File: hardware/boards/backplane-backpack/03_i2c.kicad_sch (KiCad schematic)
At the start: 13 parts, among them J11 backplane_mate, U2 TCA9548APWR

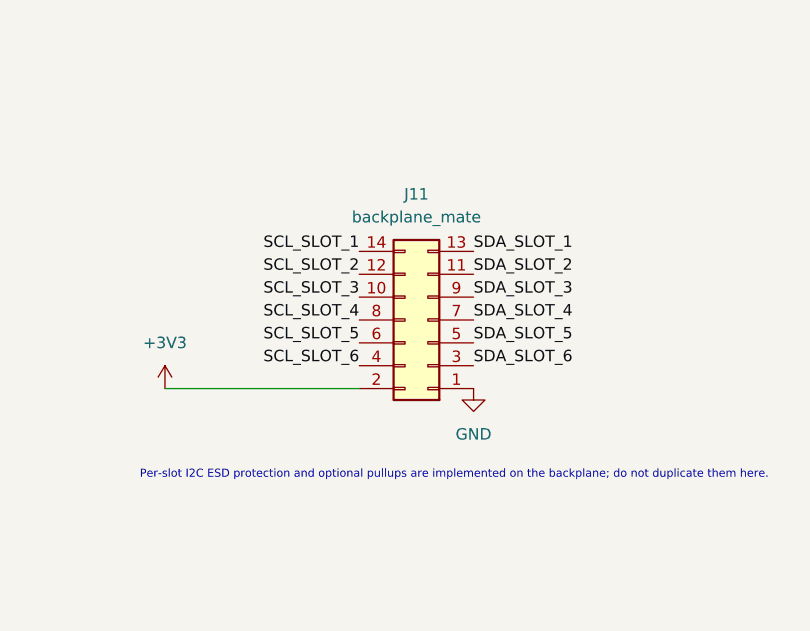
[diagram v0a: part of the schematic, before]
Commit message: feat: connect slot power controls
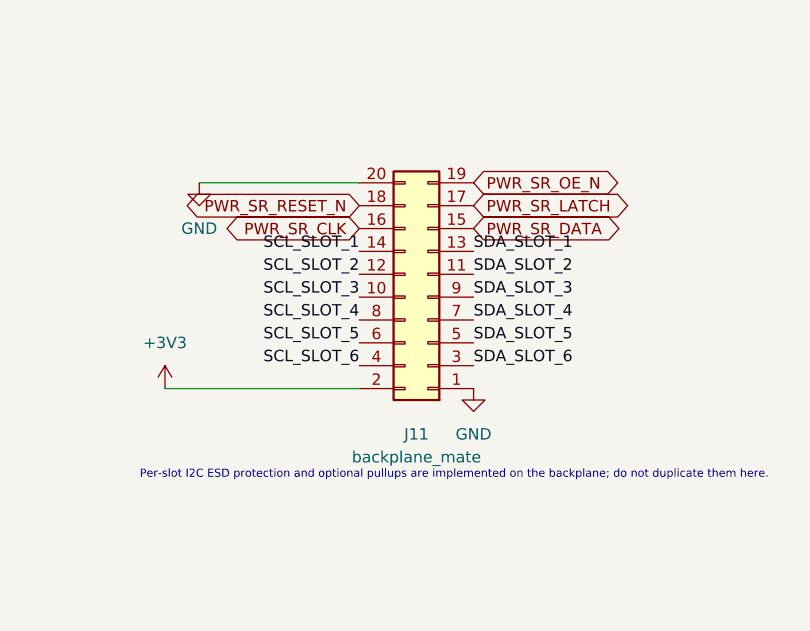
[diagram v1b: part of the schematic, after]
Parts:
- J11: footprint Connector_PinSocket_1.00mm:PinSocket_2x07_P1.00mm_Vertical_SMD -> Connector_PinSocket_1.00mm:PinSocket_2x10_P1.00mm_Vertical_SMD; symbol Connector_Generic:Conn_02x07_Odd_Even -> Connector_Generic:Conn_02x10_Odd_Even
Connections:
- net GND: now also J11.20 (Pin_20)
- new net PWR_SR_CLK: J11.16 (Pin_16)
- new net PWR_SR_DATA: J11.15 (Pin_15)
- new net PWR_SR_LATCH: J11.17 (Pin_17)
- new net PWR_SR_OE_N: J11.19 (Pin_19)
- new net PWR_SR_RESET_N: J11.18 (Pin_18)
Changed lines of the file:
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@@
+		)
+	)
+	(wire
+		(pts
+			(xy 144.78 33.02) (xy 127 33.02)
+		)
+		(stroke
+			(width 0)
+			(type default)
 		)
 	)
@@
 		(property "Intersheetrefs" "${INTERSHEET_REFS}"
 			(at 21.59 58.42 0)
+			(hide yes)
+			(show_name no)
+			(do_not_autoplace no)
+			(effects
+				(font
+					(size 1.27 1.27)
+				)
+			)
+		)
+	)
+	(global_label "PWR_SR_DATA"
+		(shape bidirectional)
+		(at 157.48 38.1 0)
+		(effects
+			(font
+				(size 1.27 1.27)
+			)
+			(justify left)
+		)
+		(property "Intersheetrefs" "${INTERSHEET_REFS}"
+			(at 157.48 38.1 0)
+			(hide yes)
+			(show_name no)
+			(do_not_autoplace no)
+			(effects
+				(font
+					(size 1.27 1.27)
+				)
+			)
+		)
+	)
+	(global_label "PWR_SR_CLK"
+		(shape bidirectional)
+		(at 144.78 38.1 180)
+		(effects
+			(font
+				(size 1.27 1.27)
+			)
+			(justify right)
+		)
+		(property "Intersheetrefs" "${INTERSHEET_REFS}"
+			(at 144.78 38.1 0)
+			(hide yes)
+			(show_name no)
+			(do_not_autoplace no)
+			(effects
+				(font
+					(size 1.27 1.27)
+				)
+			)
+		)
+	)
+	(global_label "PWR_SR_LATCH"
+		(shape bidirectional)
+		(at 157.48 35.56 0)
+		(effects
+			(font
+				(size 1.27 1.27)
+			)
+			(justify left)
+		)
+		(property "Intersheetrefs" "${INTERSHEET_REFS}"
+			(at 157.48 35.56 0)
+			(hide yes)
+			(show_name no)
+			(do_not_autoplace no)
+			(effects
+				(font
+					(size 1.27 1.27)
+				)
+			)
+		)
+	)
+	(global_label "PWR_SR_RESET_N"
+		(shape bidirectional)
+		(at 144.78 35.56 180)
+		(effects
+			(font
+				(size 1.27 1.27)
+			)
+			(justify right)
+		)
+		(property "Intersheetrefs" "${INTERSHEET_REFS}"
+			(at 144.78 35.56 0)
+			(hide yes)
+			(show_name no)
+			(do_not_autoplace no)
+			(effects
+				(font
+					(size 1.27 1.27)
+				)
+			)
+		)
+	)
+	(global_label "PWR_SR_OE_N"
+		(shape bidirectional)
+		(at 157.48 33.02 0)
+		(effects
+			(font
+				(size 1.27 1.27)
+			)
+			(justify left)
+		)
+		(property "Intersheetrefs" "${INTERSHEET_REFS}"
+			(at 157.48 33.02 0)
 			(hide yes)
 			(show_name no)
@@
 	)
 	(symbol
-		(lib_id "Connector_Generic:Conn_02x07_Odd_Even")
-		(at 152.4 48.26 180)
+		(lib_id "power:GND")
+		(at 127 33.02 0)
+		(unit 1)
+		(body_style 1)
+		(exclude_from_sim no)
+		(in_bom yes)
+		(on_board yes)
+		(in_pos_files yes)
+		(dnp no)
+		(fields_autoplaced yes)
+		(property "Reference" "#PWR0399"
+			(at 127 39.37 0)
+			(hide yes)
+			(show_name no)
+			(do_not_autoplace no)
+			(effects
+				(font
+					(size 1.27 1.27)
+				)
+			)
+		)
+		(property "Value" "GND"
+			(at 127 38.1 0)
+			(show_name no)
+			(do_not_autoplace no)
+			(effects
+				(font
+					(size 1.27 1.27)
+				)
+			)
+		)
+		(property "Footprint" ""
+			(at 127 33.02 0)
+			(hide yes)
+			(show_name no)
+			(do_not_autoplace no)
+			(effects
+				(font
+					(size 1.27 1.27)
+				)
+			)
+		)
+		(property "Datasheet" ""
+			(at 127 33.02 0)
+			(hide yes)
+			(show_name no)
+			(do_not_autoplace no)
+			(effects
+				(font
+					(size 1.27 1.27)
+				)
+			)
+		)
+		(property "Description" "Power symbol creates a global label with name \"GND\" , ground"
+			(at 127 33.02 0)
+			(hide yes)
+			(show_name no)
+			(do_not_autoplace no)
+			(effects
+				(font
+					(size 1.27 1.27)
+				)
+			)
+		)
+		(pin "1"
+		)
+		(instances
+			(project "backplane-backpack"
+				(path "/76314aad-fff2-4237-8c4a-2dbd4e06a2e1/ab8a1052-e2e8-4dde-ab61-e7465378221c"
+					(reference "#PWR0399")
+					(unit 1)
+				)
+			)
+		)
+	)
+	(symbol
+		(lib_id "Connector_Generic:Conn_02x10_Odd_Even")
+		(at 152.4 45.72 180)
 		(unit 1)
 		(body_style 1)
@@
 		(fields_autoplaced yes)
 		(property "Reference" "J11"
-			(at 151.13 34.29 0)
+			(at 151.13 60.96 0)
 			(show_name no)
 			(do_not_autoplace no)
@@
 		)
 		(property "Value" "backplane_mate"
-			(at 151.13 36.83 0)
-			(show_name no)
-			(do_not_autoplace no)
-			(effects
-				(font
-					(size 1.27 1.27)
-				)
-			)
-		)
-		(property "Footprint" "Connector_PinSocket_1.00mm:PinSocket_2x07_P1.00mm_Vertical_SMD"
-			(at 152.4 48.26 0)
+			(at 151.13 63.5 0)
+			(show_name no)
+			(do_not_autoplace no)
+			(effects
+				(font
+					(size 1.27 1.27)
+				)
+			)
+		)
+		(property "Footprint" "Connector_PinSocket_1.00mm:PinSocket_2x10_P1.00mm_Vertical_SMD"
+			(at 152.4 45.72 0)
 			(hide yes)
 			(show_name no)
@@
 		)
 		(property "Datasheet" ""
-			(at 152.4 48.26 0)
-			(hide yes)
-			(show_name no)
-			(do_not_autoplace no)
-			(effects
-				(font
-					(size 1.27 1.27)
-				)
-			)
-		)
-		(property "Description" "Generic connector, double row, 02x07, odd/even pin numbering scheme (row 1 odd numbers, row 2 even numbers), script generated (kicad-library-utils/schlib/autogen/connector/)"
-			(at 152.4 48.26 0)
+			(at 152.4 45.72 0)
+			(hide yes)
+			(show_name no)
+			(do_not_autoplace no)
+			(effects
+				(font
+					(size 1.27 1.27)
+				)
+			)
+		)
+		(property "Description" "Generic connector, double row, 02x10, odd/even pin numbering scheme (row 1 odd numbers, row 2 even numbers), script generated (kicad-library-utils/schlib/autogen/connector/)"
+			(at 152.4 45.72 0)
 			(hide yes)
 			(show_name no)
@@
 		(pin "14"
 		)
+		(pin "15"
+		)
+		(pin "16"
+		)
+		(pin "17"
+		)
+		(pin "18"
+		)
+		(pin "19"
+		)
+		(pin "20"
+		)
 		(instances

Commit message: chore: checkpoint current board layout
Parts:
- added TP7: I2C_UP_SDA, TestPoint:TestPoint_Pad_D1.5mm, symbol Connector:TestPoint
- added TP8: I2C_UP_SCL, TestPoint:TestPoint_Pad_D1.5mm, symbol Connector:TestPoint
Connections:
- net I2C_UP_SCL: now also TP8.1
- net I2C_UP_SDA: now also TP7.1

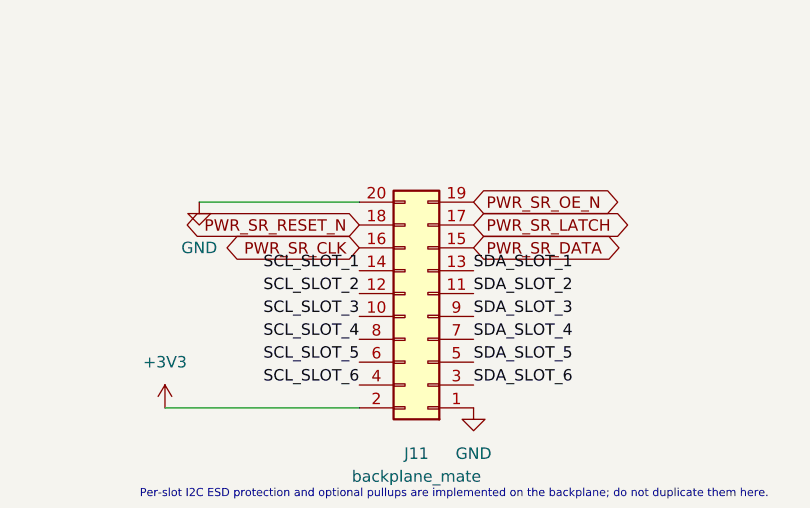
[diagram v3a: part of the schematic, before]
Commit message: Replace slot power shift register with PCA9554
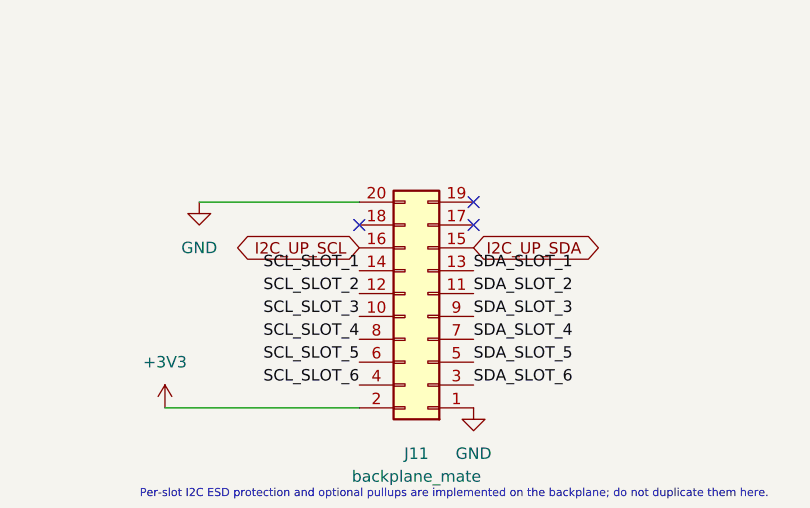
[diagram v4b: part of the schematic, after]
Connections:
- net PWR_SR_CLK is gone; now on net I2C_UP_SCL: J11.16 (Pin_16)
- net PWR_SR_DATA is gone; now on net I2C_UP_SDA: J11.15 (Pin_15)
- net PWR_SR_LATCH: no longer names the net of J11.17 (Pin_17)
- net PWR_SR_OE_N: no longer names the net of J11.19 (Pin_19)
- net PWR_SR_RESET_N: no longer names the net of J11.18 (Pin_18)
- no-connect marks 0 -> 3
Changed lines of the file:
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@@
-		)
-	)
-	(global_label "PWR_SR_OE_N"
-		(shape bidirectional)
-		(at 157.48 33.02 0)
-		(effects
-			(font
-				(size 1.27 1.27)
-			)
-			(justify left)
-		)
-		(property "Intersheetrefs" "${INTERSHEET_REFS}"
-			(at 157.48 33.02 0)
-			(hide yes)
-			(show_name no)
-			(do_not_autoplace no)
-			(effects
-				(font
-					(size 1.27 1.27)
-				)
-			)
 		)
 	)
@@
 		)
 	)
-	(global_label "PWR_SR_LATCH"
-		(shape bidirectional)
-		(at 157.48 35.56 0)
-		(effects
-			(font
-				(size 1.27 1.27)
-			)
-			(justify left)
-		)
-		(property "Intersheetrefs" "${INTERSHEET_REFS}"
-			(at 157.48 35.56 0)
-			(hide yes)
-			(show_name no)
-			(do_not_autoplace no)
-			(effects
-				(font
-					(size 1.27 1.27)
-				)
-			)
-		)
-	)
-	(global_label "PWR_SR_DATA"
+	(global_label "I2C_UP_SDA"
 		(shape bidirectional)
 		(at 157.48 38.1 0)
@@
 		)
 	)
-	(global_label "PWR_SR_CLK"
+	(global_label "I2C_UP_SCL"
 		(shape bidirectional)
 		(at 144.78 38.1 180)
@@
 		)
 	)
-	(global_label "PWR_SR_RESET_N"
-		(shape bidirectional)
-		(at 144.78 35.56 180)
-		(effects
-			(font
-				(size 1.27 1.27)
-			)
-			(justify right)
-		)
-		(property "Intersheetrefs" "${INTERSHEET_REFS}"
-			(at 144.78 35.56 0)
-			(hide yes)
-			(show_name no)
-			(do_not_autoplace no)
-			(effects
-				(font
-					(size 1.27 1.27)
-				)
-			)
-		)
+		(no_connect
+		(at 157.48 33.02)
+	)
+	(no_connect
+		(at 157.48 35.56)
+	)
+	(no_connect
+		(at 144.78 35.56)
 	)
 	(symbol

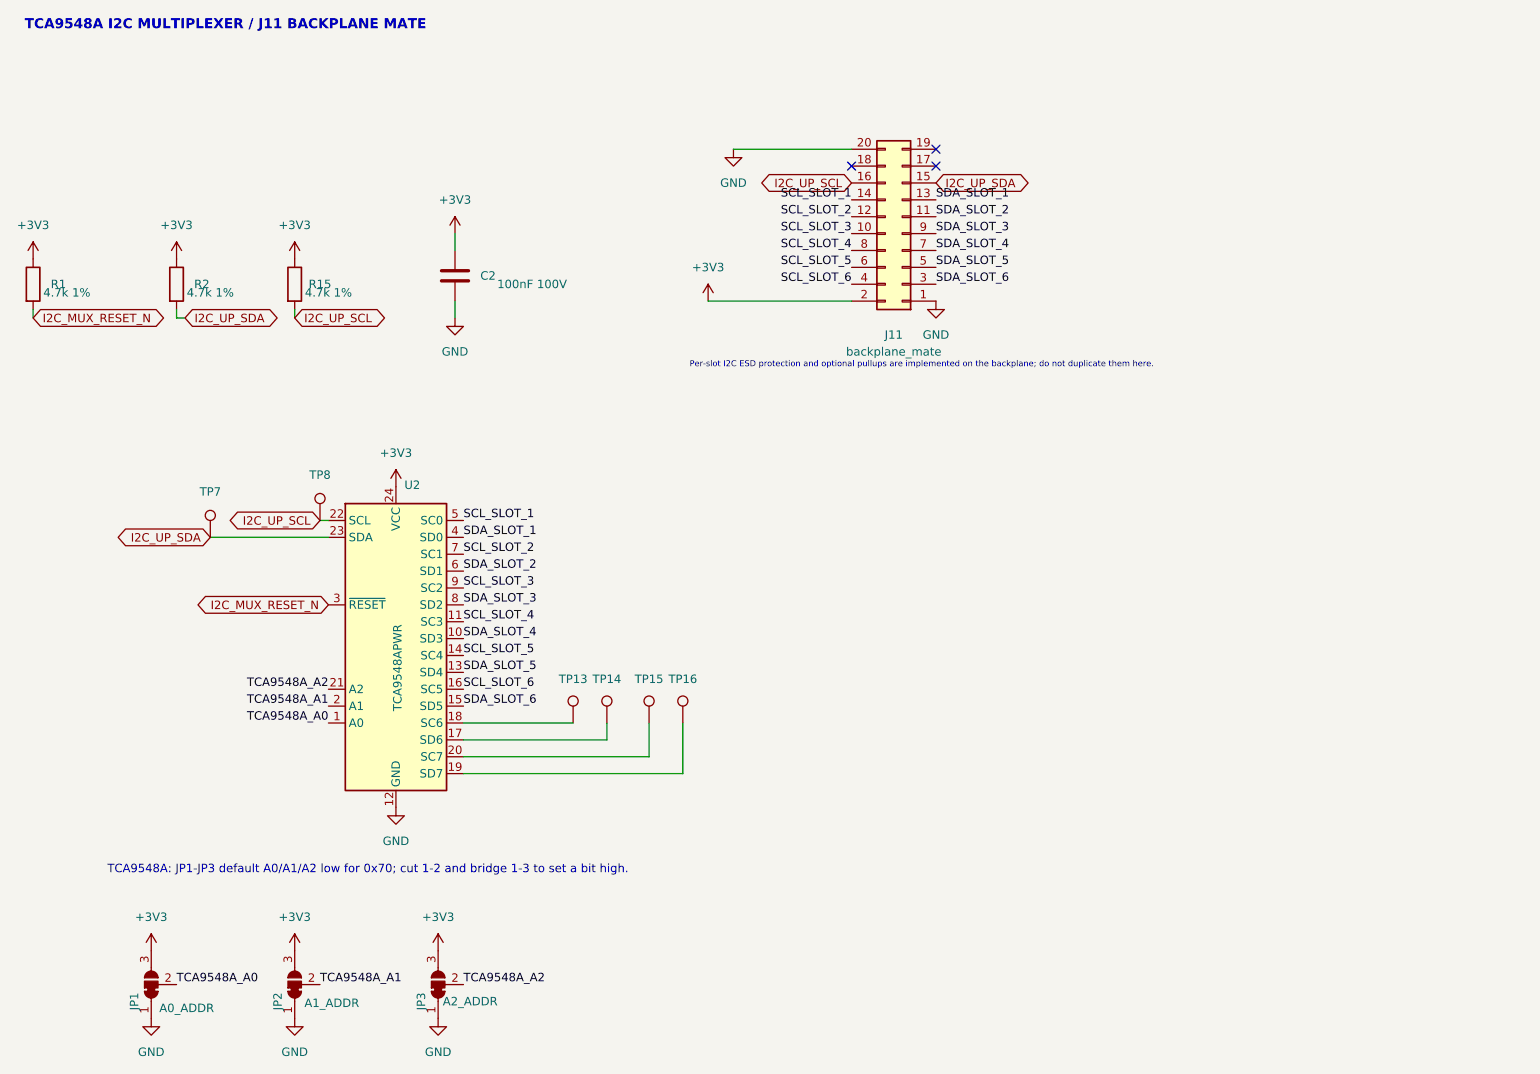
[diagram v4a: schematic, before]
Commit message: Simplify backpack backplane interface
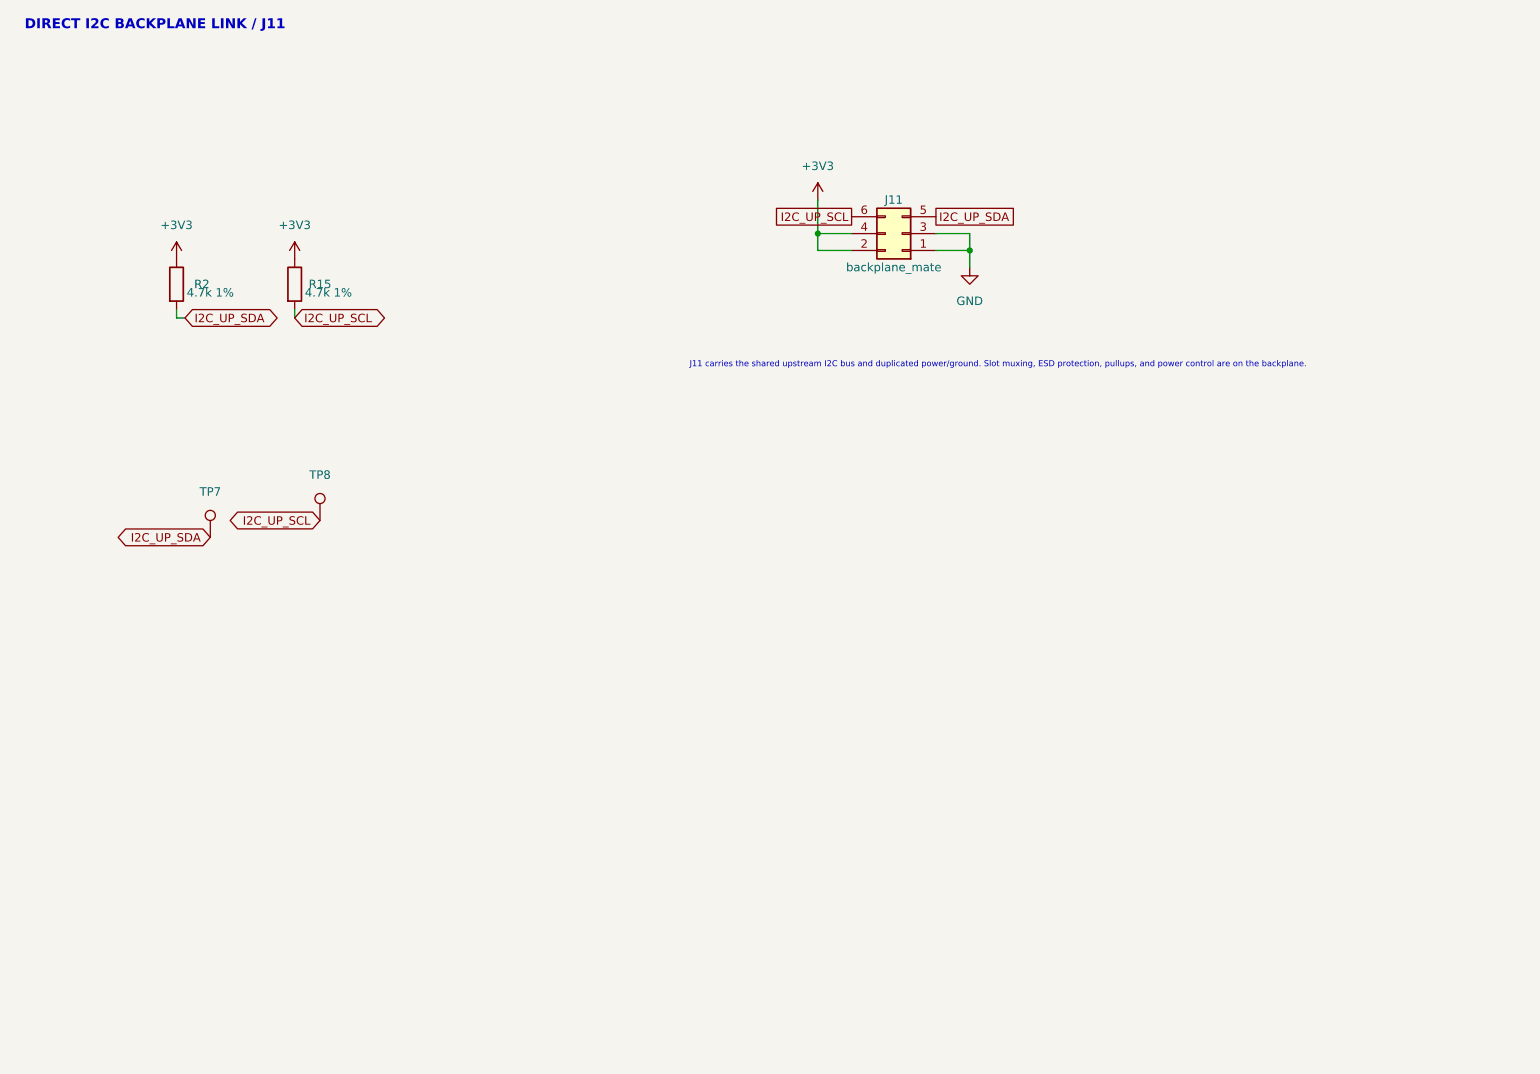
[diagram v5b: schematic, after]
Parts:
- removed C2: 100nF 100V, Capacitor_SMD:C_0603_1608Metric, symbol Device:C
- removed J11: backplane_mate, Connector_PinSocket_1.00mm:PinSocket_2x10_P1.00mm_Vertical_SMD, symbol Connector_Generic:Conn_02x10_Odd_Even
- removed JP1: A0_ADDR, Jumper:SolderJumper-3_P1.3mm_Bridged12_Pad1.0x1.5mm, symbol Jumper:SolderJumper_3_Bridged12
- removed JP2: A1_ADDR, Jumper:SolderJumper-3_P1.3mm_Bridged12_Pad1.0x1.5mm, symbol Jumper:SolderJumper_3_Bridged12
- removed JP3: A2_ADDR, Jumper:SolderJumper-3_P1.3mm_Bridged12_Pad1.0x1.5mm, symbol Jumper:SolderJumper_3_Bridged12
- removed R1: 4.7k 1%, Resistor_SMD:R_0603_1608Metric, symbol Device:R
- removed TP13, TP14, TP15, TP16: I2C6_SDA, TestPoint:TestPoint_Pad_D1.5mm, symbol Connector:TestPoint
- removed U2: TCA9548APWR, Package_SO:TSSOP-24_4.4x7.8mm_P0.65mm, symbol Interface_Expansion:TCA9548APWR
- added J11: backplane_mate, Connector_PinSocket_2.54mm:PinSocket_2x03_P2.54mm_Vertical, symbol Connector_Generic:Conn_02x03_Odd_Even
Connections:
- net +3V3: now also J11.2 (Pin_2), J11.4 (Pin_4)
- net GND: now also J11.1 (Pin_1), J11.3 (Pin_3)
- net I2C_UP_SCL: now also J11.6 (Pin_6)
- net I2C_UP_SDA: now also J11.5 (Pin_5)
- no-connect marks 3 -> 0
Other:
- note added: "DIRECT I2C BACKPLANE LINK / J11"
- note added: "J11 carries the shared upstream I2C bus and duplicated power/ground. Slot muxing, ESD protection, pullups, and power control are on the backplane."
- note removed: "Per-slot I2C ESD protection and optional pullups are implemented on the backplane; do not duplicate them here."
- note removed: "TCA9548A I2C MULTIPLEXER / J11 BACKPLANE MATE"
- note removed: "TCA9548A: JP1-JP3 default A0/A1/A2 low for 0x70; cut 1-2 and bridge 1-3 to set a bit high."

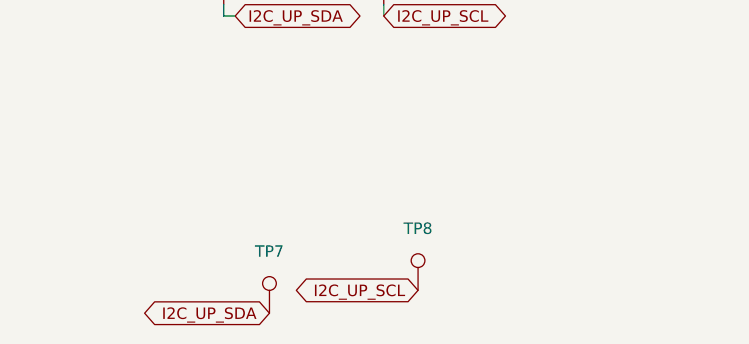
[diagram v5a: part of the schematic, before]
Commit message: hardware: mark all test points DNP
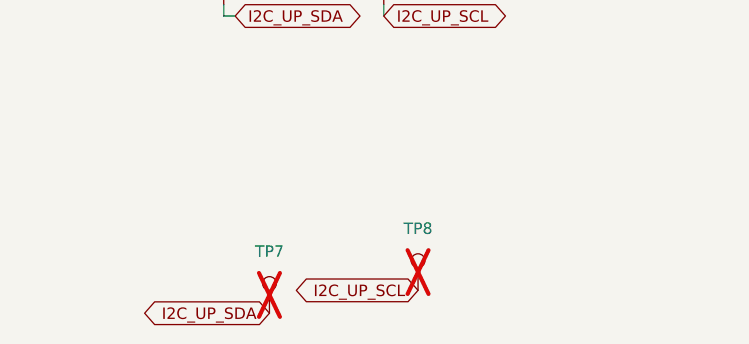
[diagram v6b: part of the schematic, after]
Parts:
- TP7, TP8: now not fitted; now left out of the parts list
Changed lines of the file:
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@@
 		(body_style 1)
 		(exclude_from_sim no)
-		(in_bom yes)
+		(in_bom no)
 		(on_board yes)
 		(in_pos_files yes)
-		(dnp no)
+		(dnp yes)
 		(property "Reference" "TP7"
 			(at 48.26 84.582 0)
@@
 		(body_style 1)
 		(exclude_from_sim no)
-		(in_bom yes)
+		(in_bom no)
 		(on_board yes)
 		(in_pos_files yes)
-		(dnp no)
+		(dnp yes)
 		(property "Reference" "TP8"
 			(at 64.77 82.042 0)
